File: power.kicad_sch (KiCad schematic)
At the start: 63 parts, among them J16 Debug connector, J17 Debug connector, J6 Debug connector, J8 Debug connector, J9 Debug connector, U2 NCP691MN33T2G

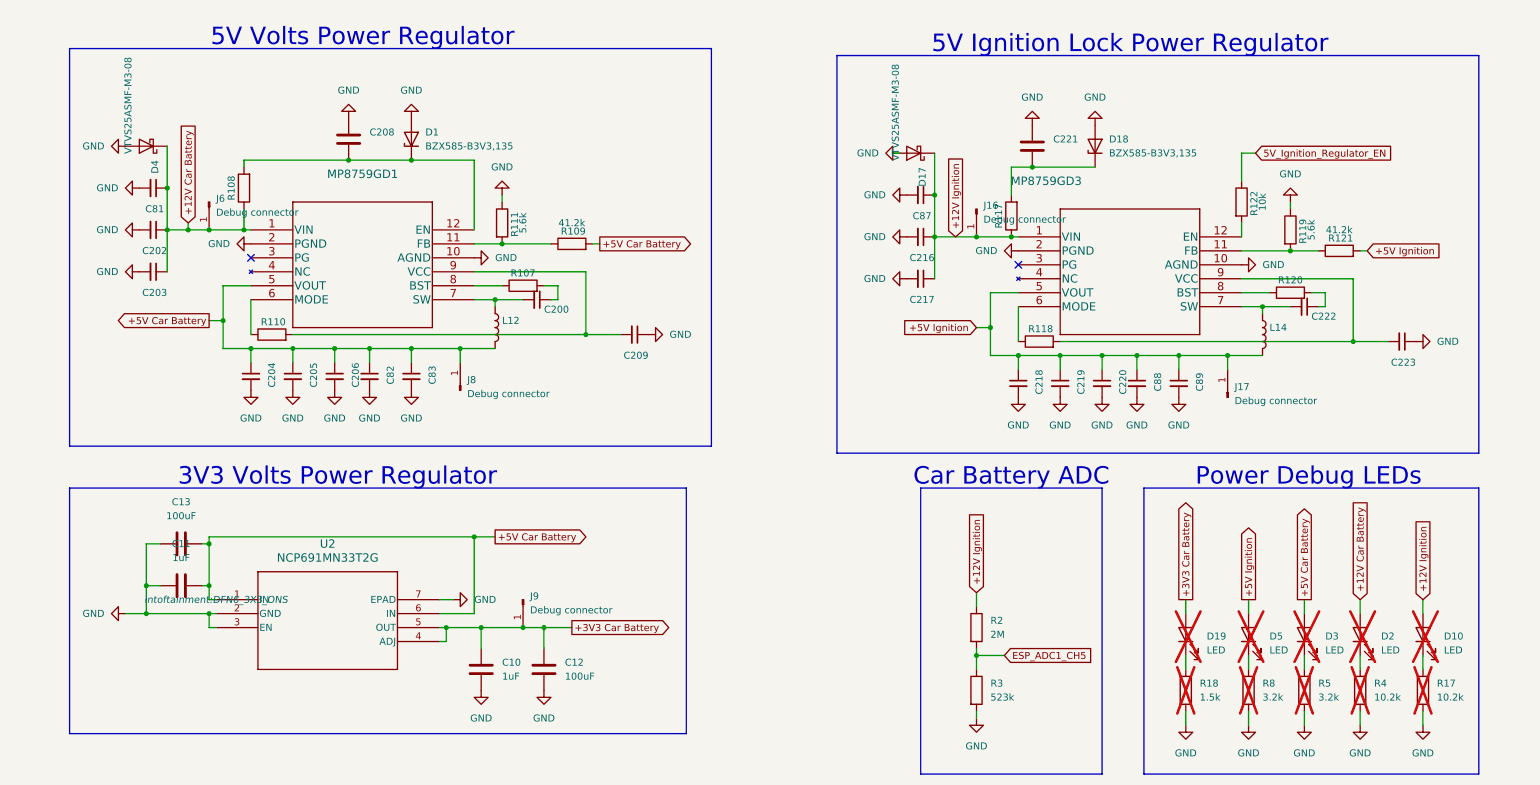
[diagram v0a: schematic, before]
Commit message: implemented the changes from 'Board defects'
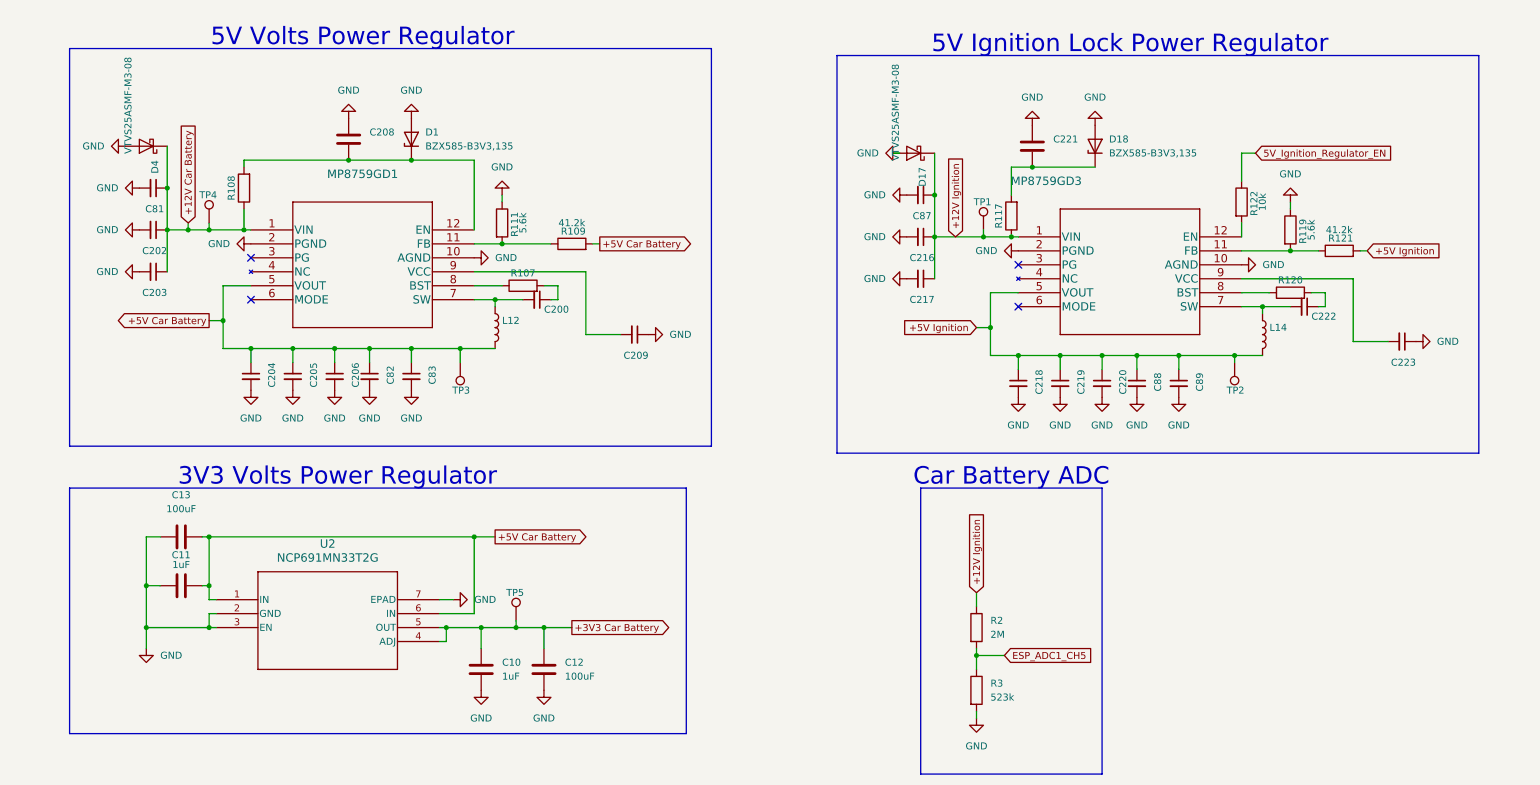
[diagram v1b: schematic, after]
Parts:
- removed D10, D19, D2, D3, D5: LED, LED_SMD:LED_0402_1005Metric, symbol Device:LED
- removed J16, J17, J6, J8, J9: Debug connector, TestPoint:TestPoint_Pad_D1.0mm, symbol Connector:Conn_01x01_Pin
- removed R110, R118: 100K, Resistor_SMD:R_0201_0603Metric, symbol Device:R
- removed R17, R4: 10.2k, Resistor_SMD:R_0805_2012Metric, symbol Device:R
- removed R18: 1.5k, Resistor_SMD:R_0805_2012Metric, symbol Device:R
- removed R5, R8: 3.2k, Resistor_SMD:R_0805_2012Metric, symbol Device:R
- added TP1, TP2, TP3, TP4, TP5: TestPoint, TestPoint:TestPoint_Pad_D1.0mm, symbol Connector:TestPoint
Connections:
- net +12V Car Battery: now also TP4.1
- net +12V Ignition: now also TP1.1
- net +3V3 Car Battery: now also TP5.1
- net +5V Car Battery: now also TP3.1
- net +5V Ignition: now also TP2.1
- no-connect marks 2 -> 4
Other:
- note removed: "Power Debug LEDs"
- moved on the sheet: C13

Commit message: 2 layer PCB
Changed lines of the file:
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@@
 	)
 	(global_label "+5V Car Battery"
-		(shape output)
+		(shape input)
 		(at 99.06 106.68 0)
 		(fields_autoplaced yes)
@@
 	)
 	(global_label "+3V3 Car Battery"
-		(shape output)
+		(shape input)
 		(at 113.03 123.19 0)
 		(fields_autoplaced yes)
@@
 		)
 		(property "Intersheetrefs" "${INTERSHEET_REFS}"
-			(at 133.0435 123.19 0)
+			(at 132.9484 123.19 0)
 			(effects
 				(font
@@
 	)
 	(global_label "+5V Car Battery"
-		(shape output)
+		(shape input)
 		(at 118.11 53.34 0)
 		(fields_autoplaced yes)
@@
 		)
 		(property "Intersheetrefs" "${INTERSHEET_REFS}"
-			(at 136.914 53.34 0)
+			(at 136.8189 53.34 0)
 			(effects
 				(font
@@
 	)
 	(global_label "+5V Car Battery"
-		(shape output)
+		(shape input)
 		(at 46.99 67.31 180)
 		(fields_autoplaced yes)
@@
 		)
 		(property "Intersheetrefs" "${INTERSHEET_REFS}"
-			(at 28.186 67.31 0)
+			(at 28.2811 67.31 0)
 			(effects
 				(font

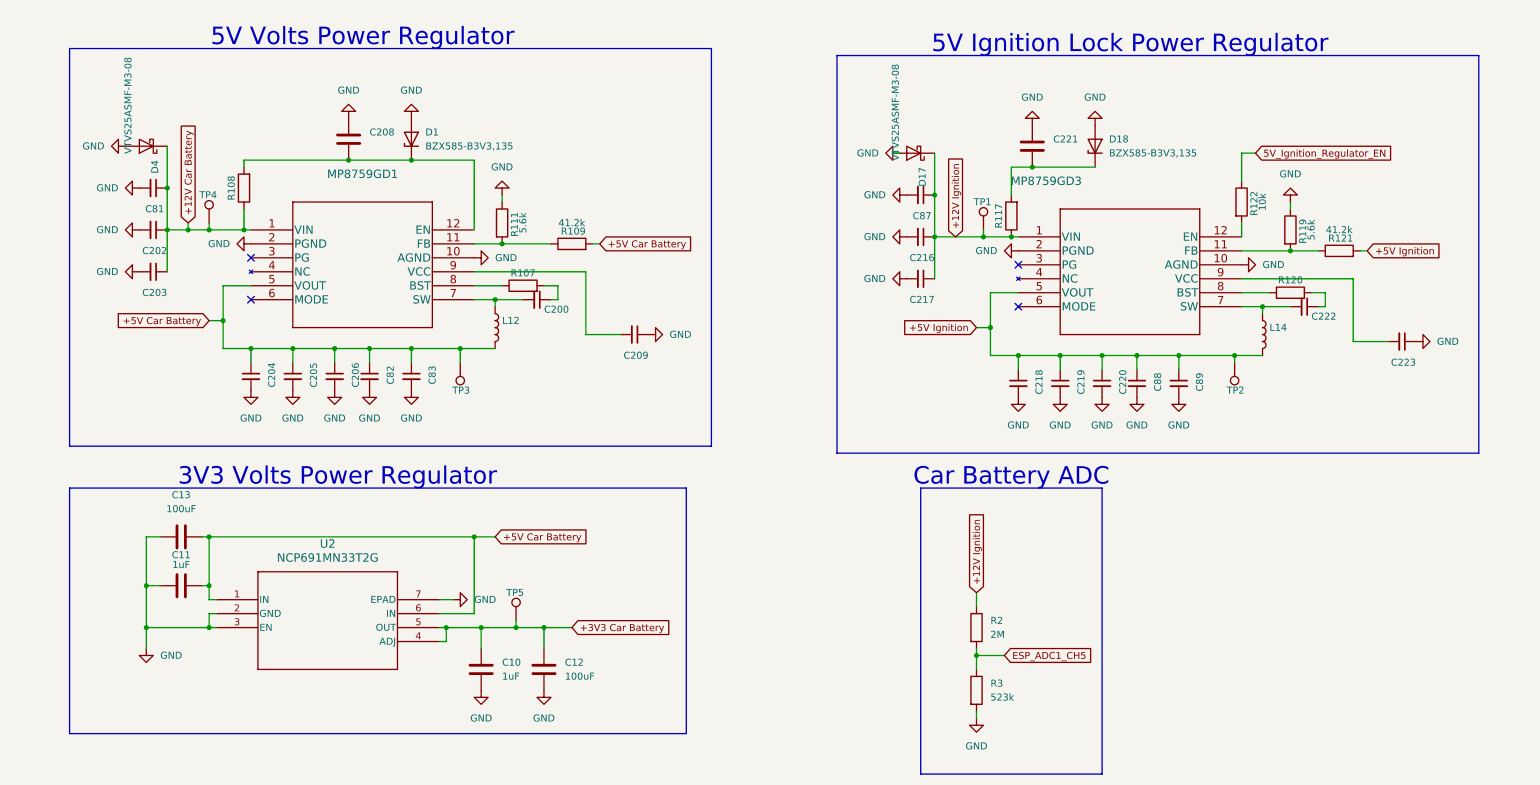
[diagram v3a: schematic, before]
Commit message: changed power regulators, updated PCB
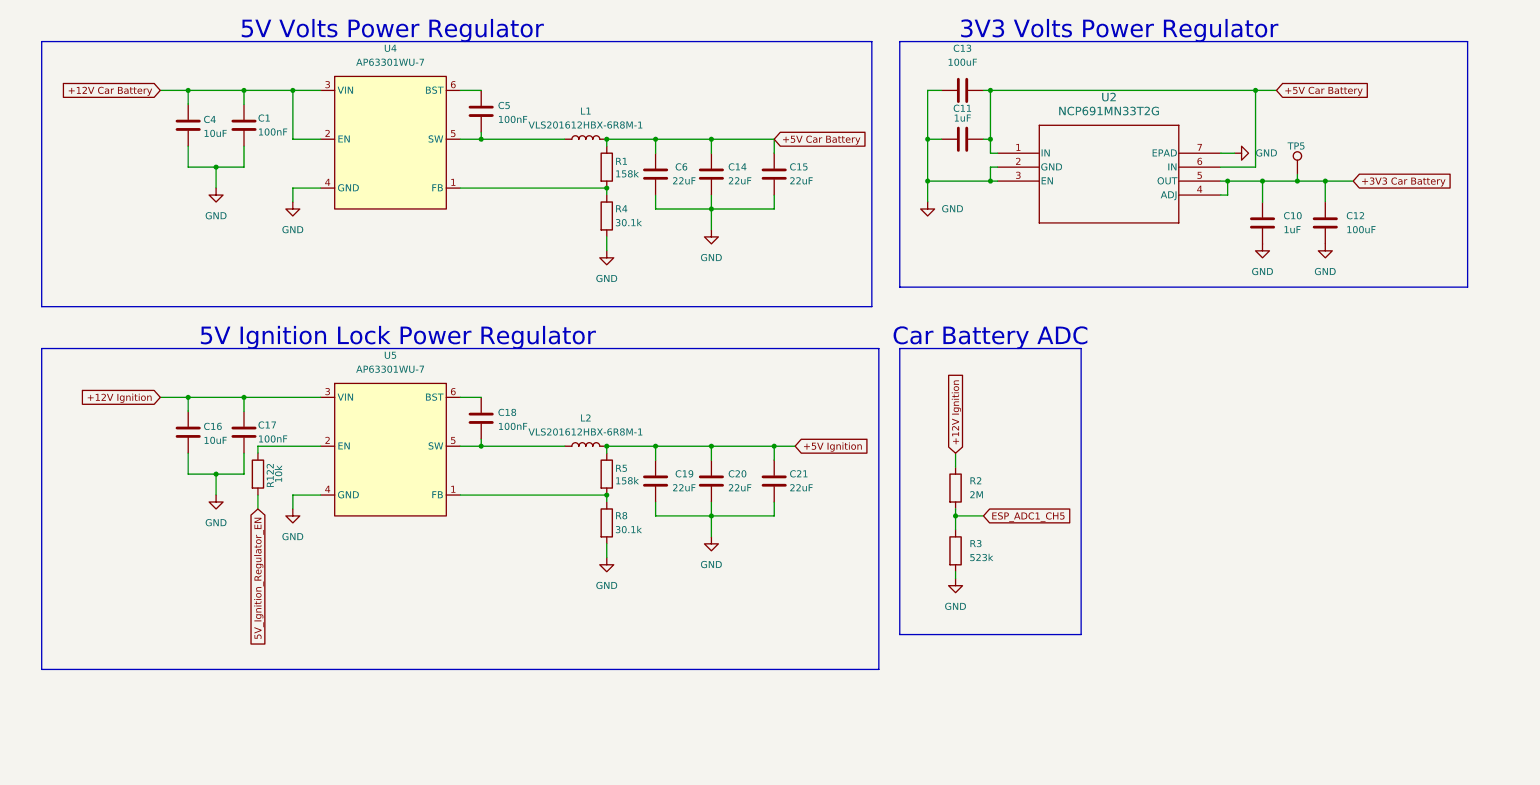
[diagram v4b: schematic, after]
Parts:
- removed C200, C222: 220nF, Capacitor_SMD:C_0603_1608Metric, symbol Device:C_Small
- removed C202, C205, C206, C216, C219, C220, C81, C82, C83, C87, C88, C89: 22uF, Capacitor_SMD:C_0805_2012Metric, symbol Device:C_Small
- removed C203, C204, C217, C218: 100nF, Capacitor_SMD:C_0402_1005Metric, symbol Device:C_Small
- removed C208, C221: 220nF, Capacitor_SMD:C_0201_0603Metric, symbol Device:C
- removed C209, C223: 1uF, Capacitor_SMD:C_0402_1005Metric, symbol Device:C_Small
- removed D1, D18: BZX585-B3V3,135, Diode_SMD:D_SOD-523, symbol Diode:DZ2S160X0L
- removed D17, D4: VTVS25ASMF-M3-08, Diode_SMD:Nexperia_CFP3_SOD-123W, symbol Diode:PMEG40T10ER
- removed L12, L14: 1.5uH, intoftainment:IND_XGL4030_COC, symbol Device:L
- removed MP8759GD1, MP8759GD3: C200, intoftainment:QFN-12_MP8759_MNP, symbol 2025-04-02_17-52-17:MP8759GD-Z
- removed R107, R120: 3.3, Resistor_SMD:R_0603_1608Metric, symbol Device:R
- removed R108, R117: 10k, Resistor_SMD:R_0201_0603Metric, symbol Device:R
- removed R109, R121: 41.2k, Resistor_SMD:R_0201_0603Metric, symbol Device:R
- removed R111, R119: 5.6k, Resistor_SMD:R_0201_0603Metric, symbol Device:R
- removed TP1, TP2, TP3, TP4: TestPoint, TestPoint:TestPoint_Pad_D1.0mm, symbol Connector:TestPoint
- added C1, C17, C18, C5: 100nF, Capacitor_SMD:C_0805_2012Metric, symbol Device:C
- added C14, C15, C19, C20, C21, C6: 22uF, Capacitor_SMD:C_0805_2012Metric, symbol Device:C
- added C16, C4: 10uF, Capacitor_SMD:C_0805_2012Metric, symbol Device:C
- added L1, L2: VLS201612HBX-6R8M-1, Inductor_SMD:L_Cenker_CKCS201610, symbol Device:L
- added R1, R5: 158k, Resistor_SMD:R_0805_2012Metric, symbol Device:R
- added R4, R8: 30.1k, Resistor_SMD:R_0805_2012Metric, symbol Device:R
- added U4, U5: AP63301WU-7, Package_TO_SOT_SMD:TSOT-23-6, symbol infotainment:ap63301wu-7
- R122: footprint Resistor_SMD:R_0201_0603Metric -> Resistor_SMD:R_0805_2012Metric
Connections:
- net +12V Car Battery: now also C1.1, C4.1, U4.2 (EN), U4.3 (VIN)
- net +12V Ignition: now also C16.1, C17.1, U5.3 (VIN)
- net +5V Car Battery: now also C14.1, C15.1, C6.1, L1.2, R1.1
- net +5V Ignition: now also C19.1, C20.1, C21.1, L2.2, R5.1
- net 5V_Ignition_Regulator_EN: now also R122.2; no longer R122.1
- net GND: now also C1.2, C14.2, C15.2, C16.2, C17.2, C19.2, C20.2, C21.2, C4.2, C6.2, R4.2, R8.2, U4.4 (GND), U5.4 (GND)
- new net: C5.2, L1.1, U4.5 (SW)
- new net: R5.2, R8.1, U5.1 (FB)
- new net: R122.1, U5.2 (EN)
- new net: C18.2, L2.1, U5.5 (SW)
- new net: C18.1, U5.6 (BST)
- new net: R1.2, R4.1, U4.1 (FB)
- new net: C5.1, U4.6 (BST)
- no-connect marks 4 -> 0
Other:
- title: (none) -> Power regulator circuit
- moved on the sheet: C10, C11, C12, C13, R122, R2, R3, TP5, U2
